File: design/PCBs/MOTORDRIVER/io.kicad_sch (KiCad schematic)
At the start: 0 parts

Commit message: worked on motor pcb
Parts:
- added J1: Screw_Terminal_01x02, symbol Connector:Screw_Terminal_01x02
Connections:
- new net BAT_12V: J1.2 (Pin_2)
- new net BAT_GND: J1.1 (Pin_1)
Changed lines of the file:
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@@
 	(generator_version "8.0")
 	(paper "A4")
+	(hierarchical_label "BAT_GND"
+		(shape input)
+		(at 133.35 91.44 180)
+		(fields_autoplaced yes)
+		(effects
+			(font
+				(size 1.27 1.27)
+			)
+			(justify right)
+		)
+	)
+	(hierarchical_label "BAT_12V"
+		(shape input)
+		(at 133.35 93.98 180)
+		(fields_autoplaced yes)
+		(effects
+			(font
+				(size 1.27 1.27)
+			)
+			(justify right)
+		)
+	)
+	(symbol
+		(lib_id "Connector:Screw_Terminal_01x02")
+		(at 138.43 91.44 0)
+		(unit 1)
+		(exclude_from_sim no)
+		(in_bom yes)
+		(on_board yes)
+		(dnp no)
+		(fields_autoplaced yes)
+		(property "Reference" "J1"
+			(at 140.97 91.4399 0)
+			(effects
+				(font
+					(size 1.27 1.27)
+				)
+				(justify left)
+			)
+		)
+		(property "Value" "Screw_Terminal_01x02"
+			(at 140.97 93.9799 0)
+			(effects
+				(font
+					(size 1.27 1.27)
+				)
+				(justify left)
+			)
+		)
+		(property "Footprint" ""
+			(at 138.43 91.44 0)
+			(effects
+				(font
+					(size 1.27 1.27)
+				)
+				(hide yes)
+			)
+		)
+		(property "Datasheet" "~"
+			(at 138.43 91.44 0)
+			(effects
+				(font
+					(size 1.27 1.27)
+				)
+				(hide yes)
+			)
+		)
+		(property "Description" "Generic screw terminal, single row, 01x02, script generated (kicad-library-utils/schlib/autogen/connector/)"
+			(at 138.43 91.44 0)
+			(effects
+				(font
+					(size 1.27 1.27)
+				)
+				(hide yes)
+			)
+		)
+		(pin "2"
+		)
+		(pin "1"
+		)
+		(instances
+			(project ""
+				(path "/c7634e88-16d1-45ec-9aac-9c841e03cf6d/38bc72d2-c2f6-4538-9c33-e1ab2a8ac987"
+					(reference "J1")
+					(unit 1)
+				)
+			)
+		)
+	)
 )

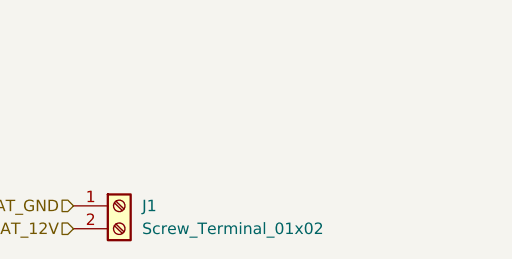
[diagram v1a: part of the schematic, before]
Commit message: Clearer file names for datasheets indicating what kind of component they are. Started on connecting the battery charger Added mosfet ICs for driver gates
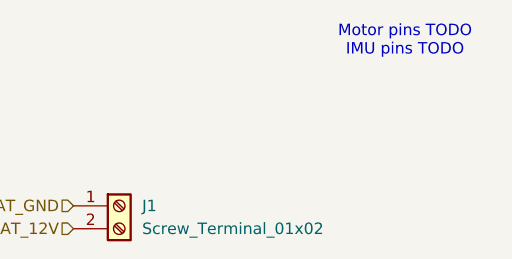
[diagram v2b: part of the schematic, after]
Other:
- note added: "Motor pins TODO IMU pins TODO"
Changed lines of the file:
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@@
 	(generator_version "8.0")
 	(paper "A4")
+	(text "Motor pins TODO\nIMU pins TODO\n"
+		(exclude_from_sim no)
+		(at 170.18 73.152 0)
+		(effects
+			(font
+				(size 1.27 1.27)
+			)
+		)
+	)
 	(hierarchical_label "BAT_GND"
 		(shape input)

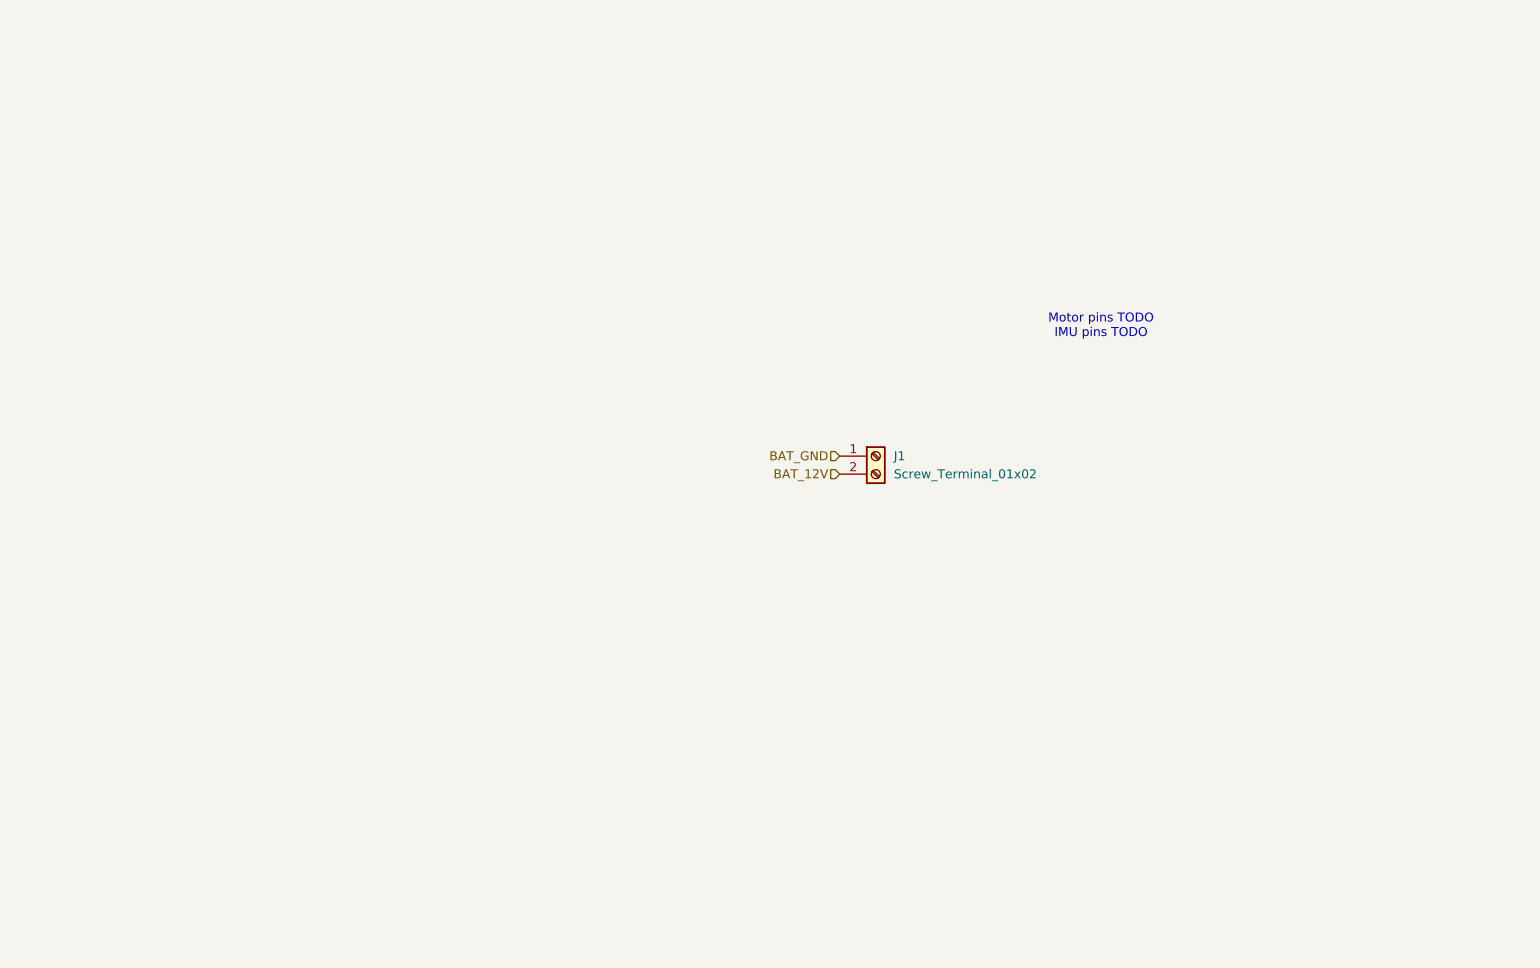
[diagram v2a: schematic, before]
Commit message: Motor headers added, mosfet datasheets
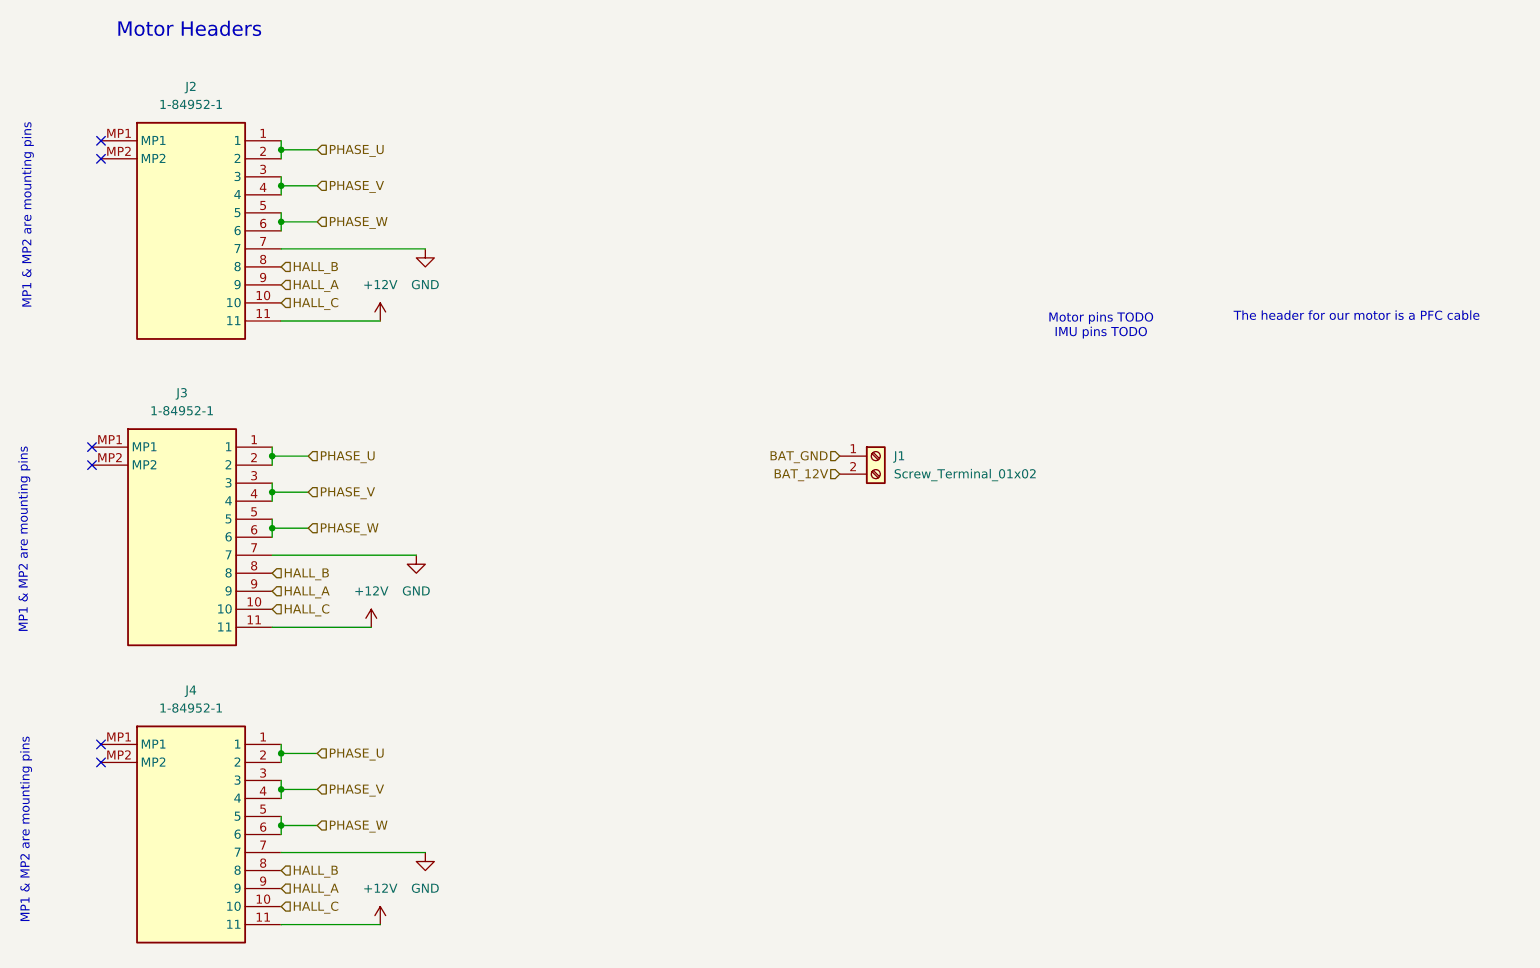
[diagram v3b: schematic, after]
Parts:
- added J2, J3, J4: 1-84952-1, 1849521, symbol 1-84952-1:1-84952-1
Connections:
- new net +12V: J2.11, J3.11, J4.11
- new net GND: J2.7, J3.7, J4.7
- new net HALL_A: J2.9, J3.9, J4.9
- new net HALL_B: J2.8, J3.8, J4.8
- new net HALL_C: J2.10, J3.10, J4.10
- new net PHASE_U: J2.1, J2.2, J3.1, J3.2, J4.1, J4.2
- new net PHASE_V: J2.3, J2.4, J3.3, J3.4, J4.3, J4.4
- new net PHASE_W: J2.5, J2.6, J3.5, J3.6, J4.5, J4.6
- no-connect marks 0 -> 6
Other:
- note added: "MP1 & MP2 are mounting pins"
- note added: "Motor Headers"
- note added: "The header for our motor is a PFC cable"
